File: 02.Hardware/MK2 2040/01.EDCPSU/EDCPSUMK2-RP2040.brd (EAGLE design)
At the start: 96 x 60.8 mm, 208 parts, among them J1 DX07S016JA1R1500, J6 Display, K1 FLEX CONNECTORES, Q2 2N7002PW, Q4 2N7002PW, Q5 2N7002PW, Q9 2N7002PW, U1 RP2040TR7, U10 IP2721, U11 AP63203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

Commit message: Version 2 revisada de la EDCPSU
Los cambios son referidos a los issues #5, #6, #7, #8, #9, #10, #11, #12.
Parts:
- D3: value BAV199 -> N.C
- FB_ADJ: value JUMPER-SMT_2_NO_NO-SILK -> JUMPER-SMT_2_NC_TRACE_NO-SILK; device SparkFun-Jumpers:SMT-JUMPER_2_NO_NO-SILK -> SparkFun-Jumpers:SMT-JUMPER_2_NC_TRACE_NO-SILK
- R11: value 10K -> 15K
- R12: value 0.05R / 1W -> 0.025R / 1W
- R15: value N.C -> 0
- R41: value 330K -> 150K
- R43: value 27K -> 11K
- R57: value 800R -> 1K
- U8: value LM4040C25FTA -> LM4040C30FTA; device LM4040C25FTA:SOT96P240X110-3N -> LM4040C30FTA:SOT96P240X120-3N
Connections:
- removed net VCC-ISO: C15.1, C8.2, U5.8
- net 3V3MCU: now also C15.1, C8.2, U5.8
- net QSPI_SD0: now also U5.5; no longer U5.2
- net QSPI_SD1: now also U5.2; no longer U5.5
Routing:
- net 3V3MCU: track 161.0 -> 171.4 mm, vias 29 -> 30
- net VCC-ISO: track 10.4 -> 0.00 mm, vias 1 -> 0
- net QSPI_SD0: track 22.3 -> 25.6 mm, vias 0 -> 2
- net QSPI_SD1: track 20.1 -> 17.8 mm, vias 2 -> 0
- net SWDIO: track 20.6 -> 19.5 mm
- added copper zone on layer 1, net N$67
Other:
- board text added: "MK2-RP2040 v2-May-2023"
- board text removed: "MK2-RP2040 v1-March-2023"

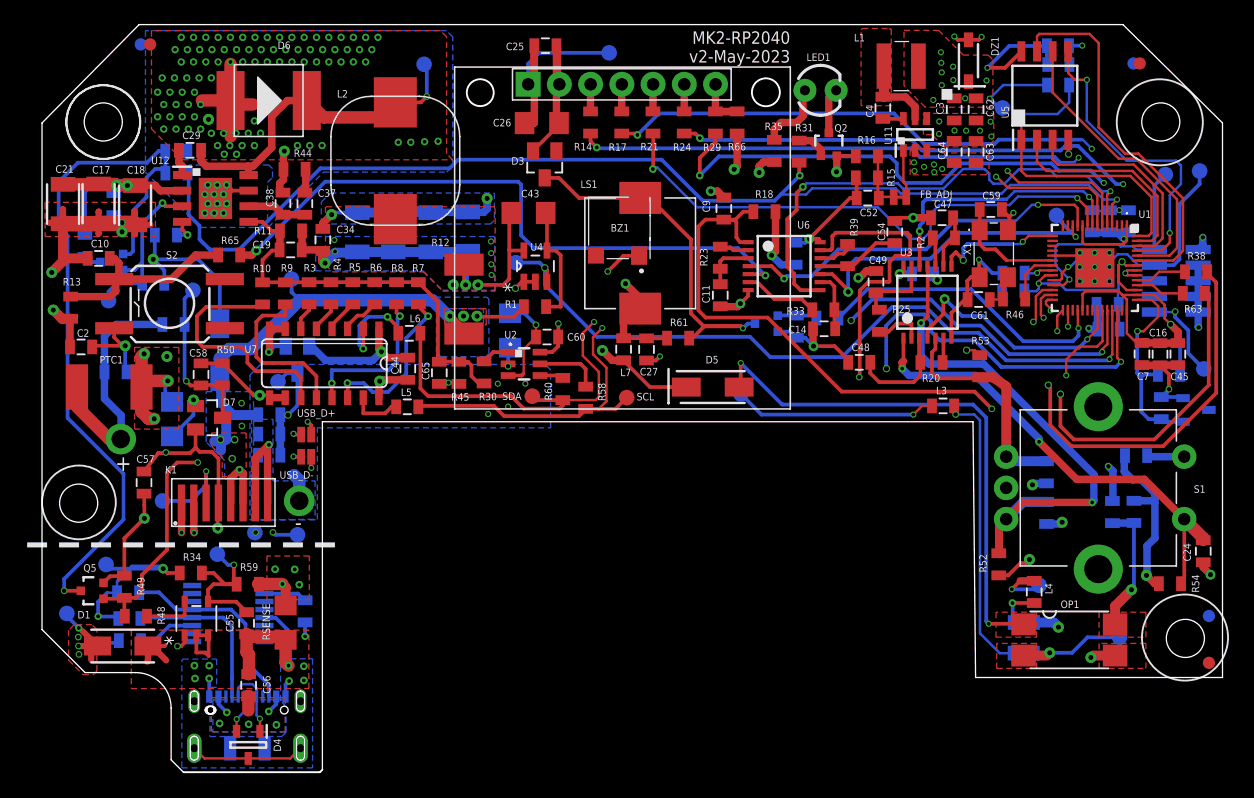
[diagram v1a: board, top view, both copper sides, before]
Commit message: Actualizacion de Cambios menores
R15 con valor 0R.
Lineas de Ref de tension a 3V_REF y R57 ajustada a 330R #10
Aumento de la linea de potencia de GND en la zona de la faja.
Mejora del marcaje de la colocacion de los Diodos.
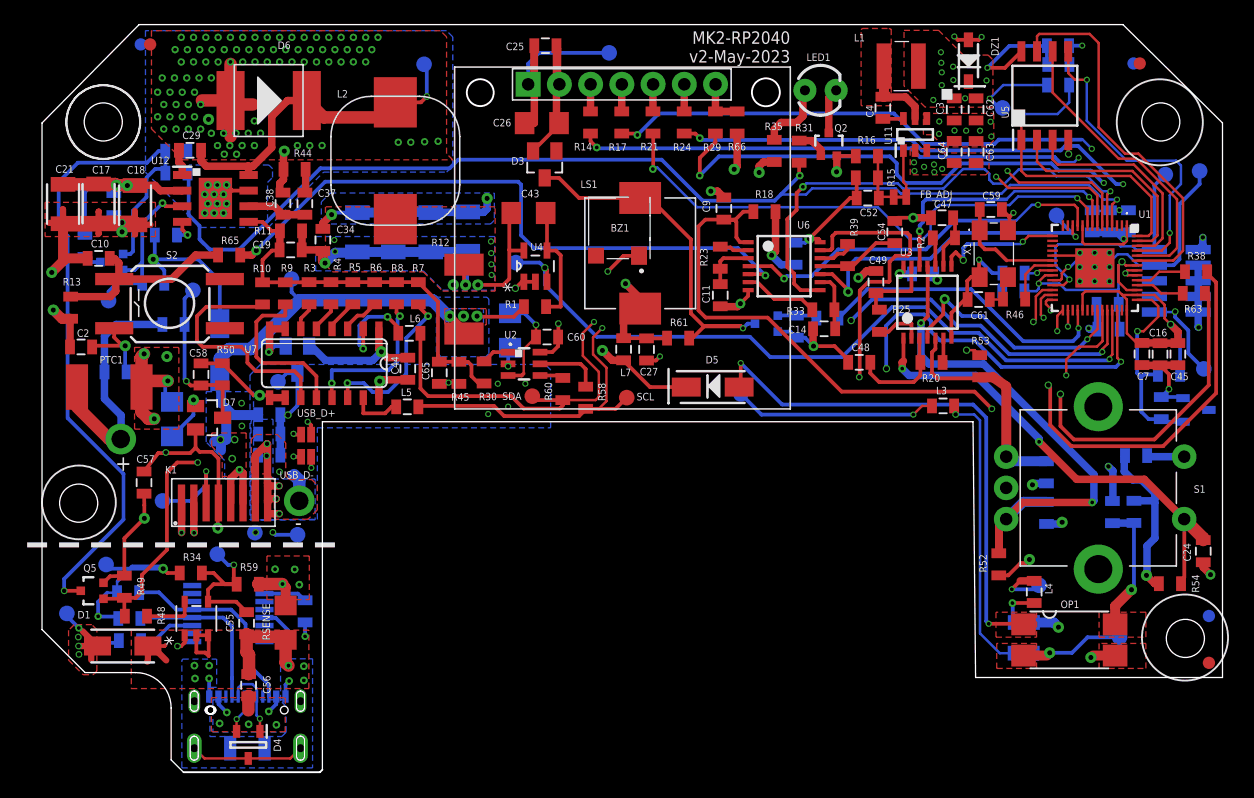
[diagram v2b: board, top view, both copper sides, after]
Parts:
- R15: value 0 -> 0R
- R57: value 1K -> 330R
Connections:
- net 2V5_REF renamed 3V_REF
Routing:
- net GND: track 229.5 -> 232.4 mm, vias 166 -> 171
- net USB_D+: track 29.4 -> 30.8 mm
- net USB_D-: track 31.6 -> 32.7 mm
- net PEDAL+: track 83.9 -> 84.8 mm

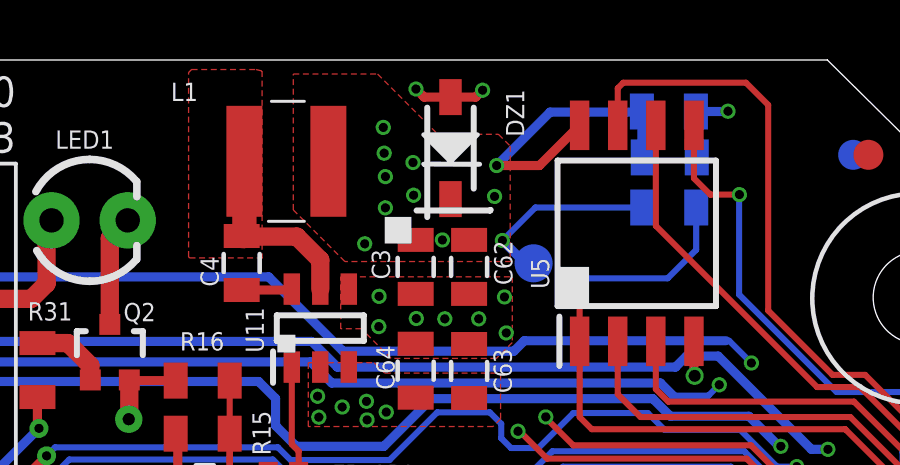
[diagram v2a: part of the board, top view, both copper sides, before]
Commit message: Update EDCPSUMK2-RP2040
Cambio del Zener del 3,6v a 3,9v. #13
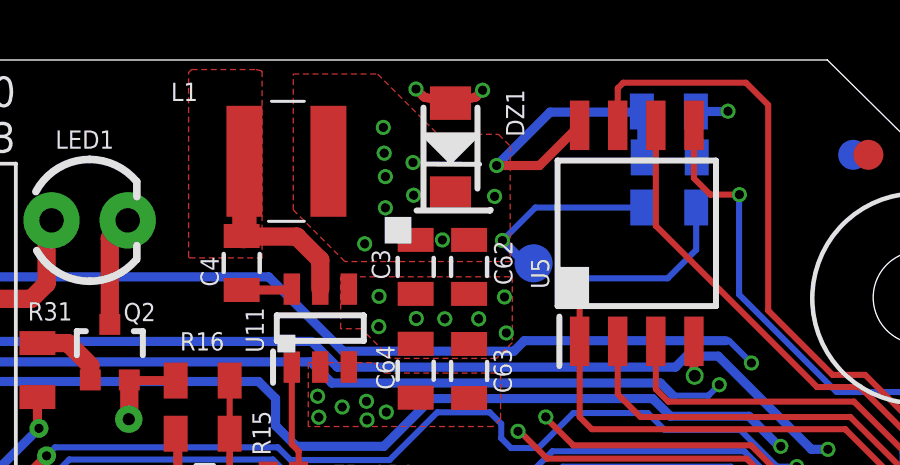
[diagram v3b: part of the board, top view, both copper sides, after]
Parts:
- DZ1: value MMSZ5227B-7-F -> MMSZ5228B-7-F; device MMSZ5227B-7-F:SOD3716X135N -> MMSZ5228B-7-F:SODFL3518X115N
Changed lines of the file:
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@@
 <drawing>
 <settings>
-<setting alwaysvectorfont="yes"/>
+<setting alwaysvectorfont="no"/>
 <setting keepoldvectorfont="yes"/>
 <setting verticaltext="up"/>
@@
 <attribute name="NAME" x="87.6645" y="63.288" size="0.6096" layer="25" font="vector" rot="R90" align="top-right"/>
 </element>
-<element name="DZ1" library="MMSZ5227B-7-F" package="SOD3716X135N" value="MMSZ5227B-7-F" x="90.14" y="69.86" smashed="yes" rot="R90">
-<attribute name="ARROW_PART_NUMBER" value="MMSZ5227B-7-F" x="90.14" y="69.86" size="1.778" layer="27" rot="R90" display="off"/>
-<attribute name="ARROW_PRICE-STOCK" value="https://www.arrow.com/en/products/mmsz5227b-7-f/diodes-incorporated" x="90.14" y="69.86" size="1.778" layer="27" rot="R90" display="off"/>
-<attribute name="DESCRIPTION" value="Diode Zener 3.6V 5% 500mW 2Pin SOD123 Diodes Inc MMSZ5227B-7-F Zener Diode, 3.6V 5% 500 mW SMT 2-Pin SOD-123" x="90.14" y="69.86" size="1.778" layer="27" rot="R90" display="off"/>
-<attribute name="HEIGHT" value="1.35mm" x="90.14" y="69.86" size="1.778" layer="27" rot="R90" display="off"/>
+<element name="DZ1" library="MMSZ5228B-7-F" package="SODFL3518X115N" value="MMSZ5228B-7-F" x="90.14" y="69.86" smashed="yes" rot="R90">
+<attribute name="ARROW_PART_NUMBER" value="" x="90.14" y="69.86" size="1.778" layer="27" rot="R90" display="off"/>
+<attribute name="ARROW_PRICE-STOCK" value="" x="90.14" y="69.86" size="1.778" layer="27" rot="R90" display="off"/>
+<attribute name="DESCRIPTION" value="Diodes Inc MMSZ5228B-7-F Zener Diode, 3.9V 5% 500 mW SMT 2-Pin SOD-123" x="90.14" y="69.86" size="1.778" layer="27" rot="R90" display="off"/>
+<attribute name="HEIGHT" value="1.15mm" x="90.14" y="69.86" size="1.778" layer="27" rot="R90" display="off"/>
 <attribute name="MANUFACTURER_NAME" value="Diodes Inc." x="90.14" y="69.86" size="1.778" layer="27" rot="R90" display="off"/>
-<attribute name="MANUFACTURER_PART_NUMBER" value="MMSZ5227B-7-F" x="90.14" y="69.86" size="1.778" layer="27" rot="R90" display="off"/>
-<attribute name="MOUSER_PART_NUMBER" value="621-MMSZ5227B-F" x="90.14" y="69.86" size="1.778" layer="27" rot="R90" display="off"/>
-<attribute name="MOUSER_PRICE-STOCK" value="https://www.mouser.com/Search/Refine.aspx?Keyword=621-MMSZ5227B-F" x="90.14" y="69.86" size="1.778" layer="27" rot="R90" display="off"/>
+<attribute name="MANUFACTURER_PART_NUMBER" value="MMSZ5228B-7-F" x="90.14" y="69.86" size="1.778" layer="27" rot="R90" display="off"/>
+<attribute name="MOUSER_PART_NUMBER" value="" x="90.14" y="69.86" size="1.778" layer="27" rot="R90" display="off"/>
+<attribute name="MOUSER_PRICE-STOCK" value="" x="90.14" y="69.86" size="1.778" layer="27" rot="R90" display="off"/>
 <attribute name="NAME" x="92.6" y="70.24" size="0.6096" layer="25" font="vector" rot="R270" align="top-right"/>
 </element>
@@
 <via x="91.21" y="71.79" extent="1-16" drill="0.3048"/>
 <wire x1="88.99" y1="71.83" x2="89.26" y2="71.56" width="0.3048" layer="1"/>
-<wire x1="89.26" y1="71.56" x2="90.14" y2="71.56" width="0.3048" layer="1"/>
-<wire x1="90.14" y1="71.56" x2="90.98" y2="71.56" width="0.3048" layer="1"/>
+<wire x1="89.26" y1="71.56" x2="90.14" y2="71.36" width="0.3048" layer="1"/>
+<wire x1="90.14" y1="71.36" x2="90.98" y2="71.56" width="0.3048" layer="1"/>
 <wire x1="90.98" y1="71.56" x2="91.21" y2="71.79" width="0.3048" layer="1"/>
 <wire x1="98.35" y1="69.55" x2="98.35" y2="71.05" width="0.3048" layer="16"/>

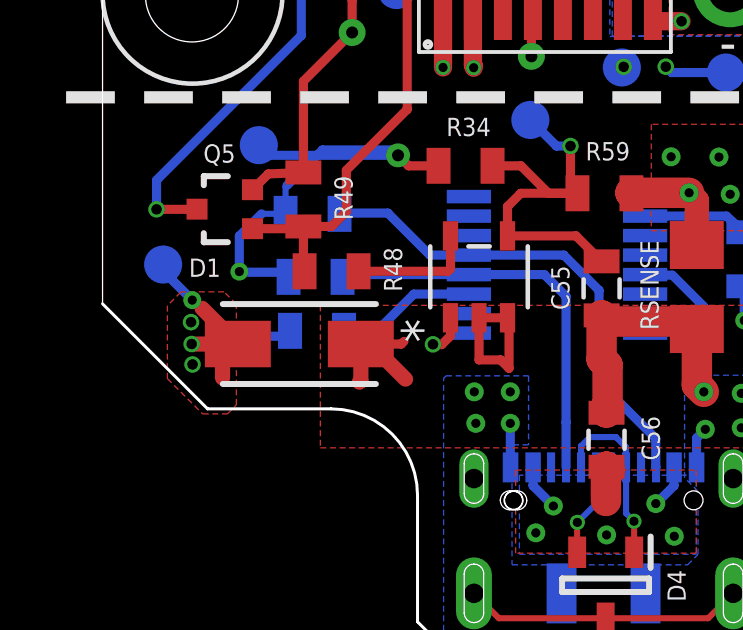
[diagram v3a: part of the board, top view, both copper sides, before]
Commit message: Update EDCPSUMK2-RP2040 - Diodo entrada D1
Cambio del diodo D1 de bidireccional a Unidireccional de 24v. #14
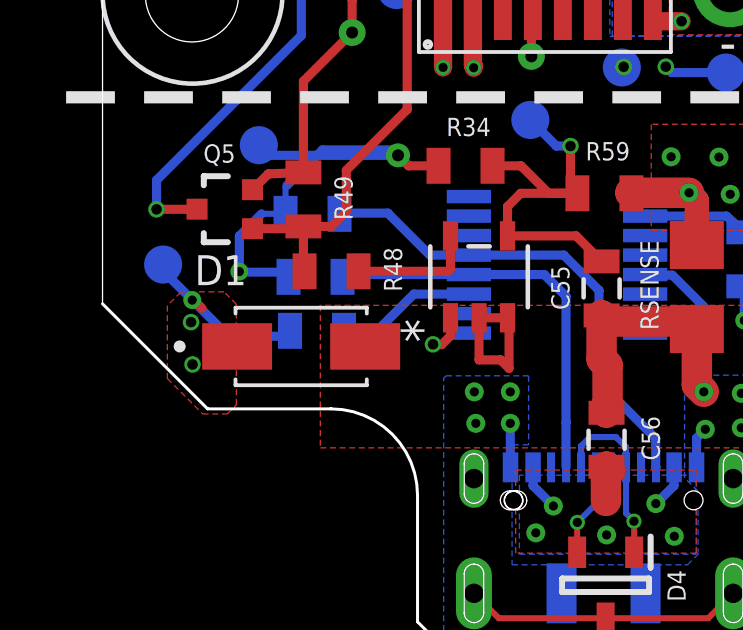
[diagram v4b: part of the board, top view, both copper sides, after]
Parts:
- D1: value SMAJ24CA -> SMAJ24A; device SMAJ24CA:DIONM5127X229N -> 3SMAJ5934B:DIOM4325X244N
- moved D1 0.10 mm to (21.4, 22.2), turned to 0 degrees
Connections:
- net GND_IN: now also D1.A; no longer D1.1
- net IN+: now also D1.C; no longer D1.2
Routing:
- net GND_IN: track 52.7 -> 47.9 mm
- net IN+: track 36.3 -> 31.7 mm, vias 11 -> 10
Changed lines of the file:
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@@
 <layers>
 <layer number="1" name="Top" color="4" fill="1" visible="yes" active="yes"/>
-<layer number="2" name="GND" color="5" fill="1" visible="yes" active="yes"/>
+<layer number="2" name="GND" color="5" fill="1" visible="no" active="yes"/>
 <layer number="3" name="Route3" color="4" fill="3" visible="no" active="no"/>
 <layer number="4" name="Route4" color="1" fill="4" visible="no" active="no"/>
@@
 <layer number="13" name="Route13" color="4" fill="5" visible="no" active="no"/>
 <layer number="14" name="Route14" color="1" fill="6" visible="no" active="no"/>
-<layer number="15" name="PWR" color="3" fill="1" visible="yes" active="yes"/>
-<layer number="16" name="Bottom" color="1" fill="1" visible="yes" active="yes"/>
+<layer number="15" name="PWR" color="3" fill="1" visible="no" active="yes"/>
+<layer number="16" name="Bottom" color="1" fill="1" visible="no" active="yes"/>
 <layer number="17" name="Pads" color="2" fill="1" visible="yes" active="yes"/>
 <layer number="18" name="Vias" color="2" fill="1" visible="yes" active="yes"/>
@@
 <layer number="20" name="Dimension" color="15" fill="1" visible="yes" active="yes"/>
 <layer number="21" name="tPlace" color="7" fill="1" visible="yes" active="yes"/>
-<layer number="22" name="bPlace" color="7" fill="1" visible="yes" active="yes"/>
+<layer number="22" name="bPlace" color="7" fill="1" visible="no" active="yes"/>
 <layer number="23" name="tOrigins" color="15" fill="1" visible="yes" active="yes"/>
-<layer number="24" name="bOrigins" color="15" fill="1" visible="yes" active="yes"/>
+<layer number="24" name="bOrigins" color="15" fill="1" visible="no" active="yes"/>
 <layer number="25" name="tNames" color="7" fill="1" visible="yes" active="yes"/>
-<layer number="26" name="bNames" color="7" fill="1" visible="yes" active="yes"/>
+<layer number="26" name="bNames" color="7" fill="1" visible="no" active="yes"/>
 <layer number="27" name="tValues" color="7" fill="1" visible="no" active="yes"/>
 <layer number="28" name="bValues" color="7" fill="1" visible="no" active="yes"/>
@@
 <layer number="38" name="bTest" color="7" fill="1" visible="no" active="yes"/>
 <layer number="39" name="tKeepout" color="4" fill="11" visible="yes" active="yes"/>
-<layer number="40" name="bKeepout" color="1" fill="11" visible="yes" active="yes"/>
+<layer number="40" name="bKeepout" color="1" fill="11" visible="no" active="yes"/>
 <layer number="41" name="tRestrict" color="4" fill="10" visible="yes" active="yes"/>
-<layer number="42" name="bRestrict" color="1" fill="10" visible="yes" active="yes"/>
+<layer number="42" name="bRestrict" color="1" fill="10" visible="no" active="yes"/>
 <layer number="43" name="vRestrict" color="2" fill="10" visible="no" active="yes"/>
 <layer number="44" name="Drills" color="7" fill="1" visible="no" active="yes"/>
@@
 <layer number="50" name="dxf" color="7" fill="1" visible="no" active="no"/>
 <layer number="51" name="tDocu" color="7" fill="1" visible="yes" active="yes"/>
-<layer number="52" name="bDocu" color="7" fill="1" visible="yes" active="yes"/>
+<layer number="52" name="bDocu" color="7" fill="1" visible="no" active="yes"/>
 <layer number="53" name="tGND_GNDA" color="7" fill="9" visible="no" active="no"/>
 <layer number="54" name="bGND_GNDA" color="1" fill="9" visible="no" active="no"/>
@@
 <attribute name="NAME" x="34.24" y="13.67" size="0.6096" layer="25" font="vector" rot="R270" align="top-right"/>
 </element>
-<element name="D1" library="SMAJ24CA" package="DIONM5127X229N" value="SMAJ24CA" x="21.36" y="22.26" smashed="yes" rot="R180">
-<attribute name="ARROW_PART_NUMBER" value="SMAJ24CA" x="22.61" y="22.26" size="1.778" layer="27" rot="R180" display="off"/>
-<attribute name="ARROW_PRICE-STOCK" value="https://www.arrow.com/en/products/smaj24ca/bourns?region=nac" x="22.61" y="22.26" size="1.778" layer="27" rot="R180" display="off"/>
-<attribute name="DESCRIPTION" value="ESD Suppressors / TVS Diodes 24volts 5uA 10.3 Amps Bi-Dir" x="22.61" y="22.26" size="1.778" layer="27" rot="R180" display="off"/>
-<attribute name="HEIGHT" value="2.29mm" x="22.61" y="22.26" size="1.778" layer="27" rot="R180" display="off"/>
-<attribute name="MANUFACTURER_NAME" value="Bourns" x="22.61" y="22.26" size="1.778" layer="27" rot="R180" display="off"/>
-<attribute name="MANUFACTURER_PART_NUMBER" value="SMAJ24CA" x="22.61" y="22.26" size="1.778" layer="27" rot="R180" display="off"/>
-<attribute name="MOUSER_PART_NUMBER" value="652-SMAJ24CA" x="22.61" y="22.26" size="1.778" layer="27" rot="R180" display="off"/>
-<attribute name="MOUSER_PRICE-STOCK" value="https://www.mouser.co.uk/ProductDetail/Bourns/SMAJ24CA?qs=A3H9pljuJ8RsSQb8zLkILA%3D%3D" x="22.61" y="22.26" size="1.778" layer="27" rot="R180" display="off"/>
-<attribute name="NAME" x="17.68" y="24.5" size="0.6096" layer="25" font="vector" rot="R180" align="top-right"/>
-</element>
 <element name="R30" library="SparkFun-Resistors" library_urn="urn:adsk.eagle:library:532" package="0805" package3d_urn="urn:adsk.eagle:package:39651/1" value="N.C" x="50.75" y="44.51" smashed="yes" rot="R270">
 <attribute name="NAME" x="51.798" y="42.8555" size="0.6096" layer="25" font="vector" align="top-right"/>
@@
 <attribute name="VALUE" x="25.235" y="33.298" size="0.0254" layer="28" rot="MR0"/>
 </element>
+<element name="D1" library="3SMAJ5934B" package="DIOM4325X244N" value="SMAJ24A" x="21.42" y="22.18" smashed="yes">
+<attribute name="AVAILABILITY" value="Not in stock" x="21.42" y="22.18" size="1.778" layer="27" display="off"/>
+<attribute name="DESCRIPTION" value=" Zener Diode Single 24V 5% 19Ohm 3000mW 2-Pin SMA T/R " x="21.42" y="22.18" size="1.778" layer="27" display="off"/>
+<attribute name="MF" value="Micro Commercial Components" x="21.42" y="22.18" size="1.778" layer="27" display="off"/>
+<attribute name="MP" value="3SMAJ5934B" x="21.42" y="22.18" size="1.778" layer="27" display="off"/>
+<attribute name="NAME" x="17.87" y="24.2225" size="1" layer="25"/>
+<attribute name="PACKAGE" value="None" x="21.42" y="22.18" size="1.778" layer="27" display="off"/>
+<attribute name="PRICE" value="None" x="21.42" y="22.18" size="1.778" layer="27" display="off"/>
+<attribute name="VALUE" x="17.87" y="20.1375" size="1" layer="27" align="top-left"/>
+</element>
 </elements>
 <signals>
@@
 <wire x1="31.57" y1="13.12" x2="28.01" y2="13.12" width="0.2032" layer="1"/>
 <wire x1="28.01" y1="13.12" x2="27.18" y2="13.95" width="0.2032" layer="1"/>
-<contactref element="D1" pad="1"/>
 <wire x1="20.95" y1="27.55" x2="20.9" y2="27.5" width="0.2032" layer="16"/>
 <wire x1="20.9" y1="27.5" x2="20.9" y2="26.6" width="0.2032" layer="16"/>
 <wire x1="20.9" y1="26.6" x2="20.1" y2="26.6" width="0.2032" layer="16"/>
-<wire x1="23.41" y1="22.26" x2="24.76" y2="22.26" width="0.3048" layer="1"/>
-<wire x1="24.76" y1="22.26" x2="24.85" y2="22.35" width="0.3048" layer="1"/>
-<wire x1="23.41" y1="22.26" x2="23.41" y2="21.04" width="0.508" layer="1"/>
-<wire x1="23.41" y1="21.04" x2="23.36" y2="20.99" width="0.508" layer="1"/>
-<wire x1="23.41" y1="22.26" x2="23.73" y2="22.26" width="0.508" layer="1"/>
-<wire x1="23.73" y1="22.26" x2="24.9" y2="21.09" width="0.508" layer="1"/>
 <contactref element="GND_IN" pad="TP"/>
 <wire x1="24.65" y1="28.55" x2="20.35" y2="28.55" width="0.3048" layer="16"/>
 <wire x1="20.35" y1="28.55" x2="20.01" y2="28.89" width="0.3048" layer="16"/>
+<contactref element="D1" pad="A"/>
 </signal>
 <signal name="IN+">
@@
 <vertex x="22.68" y="40.87"/>
 </polygon>
-<contactref element="D1" pad="2"/>
 <contactref element="J1" pad="2"/>
 <contactref element="J1" pad="11"/>
@@
 <wire x1="17.6423" y1="41.7139" x2="20.2662" y2="39.09" width="1.016" layer="1"/>
 <via x="17.75" y="22.99" extent="1-16" drill="0.35"/>
-<via x="17.77" y="22.26" extent="1-16" drill="0.35"/>
 <via x="17.8" y="21.58" extent="1-16" drill="0.35"/>
 <polygon width="0.0762" layer="1" isolate="0.3048">
@@
 <vertex x="17.43" y="24"/>
 </polygon>
-<wire x1="19.31" y1="22.26" x2="17.77" y2="22.26" width="0.508" layer="1"/>
-<wire x1="19.31" y1="22.26" x2="18.8" y2="21.75" width="0.508" layer="1"/>
-<wire x1="18.8" y1="21.75" x2="18.8" y2="21.13" width="0.508" layer="1"/>
-<wire x1="19.31" y1="22.26" x2="18.12" y2="23.45" width="0.508" layer="1"/>
 <contactref element="IN+" pad="TP"/>
 <wire x1="16.82" y1="24.91" x2="16.82" y2="24.695" width="0.3048" layer="16"/>
 <wire x1="16.82" y1="24.695" x2="17.79" y2="23.725" width="0.3048" layer="16"/>
+<contactref element="D1" pad="C"/>
 </signal>
 <signal name="CC1">
